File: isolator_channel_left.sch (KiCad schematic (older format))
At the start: 44 parts, among them U201 NE5532, U202 NE5532, U203 NE5532, U204 NE5532

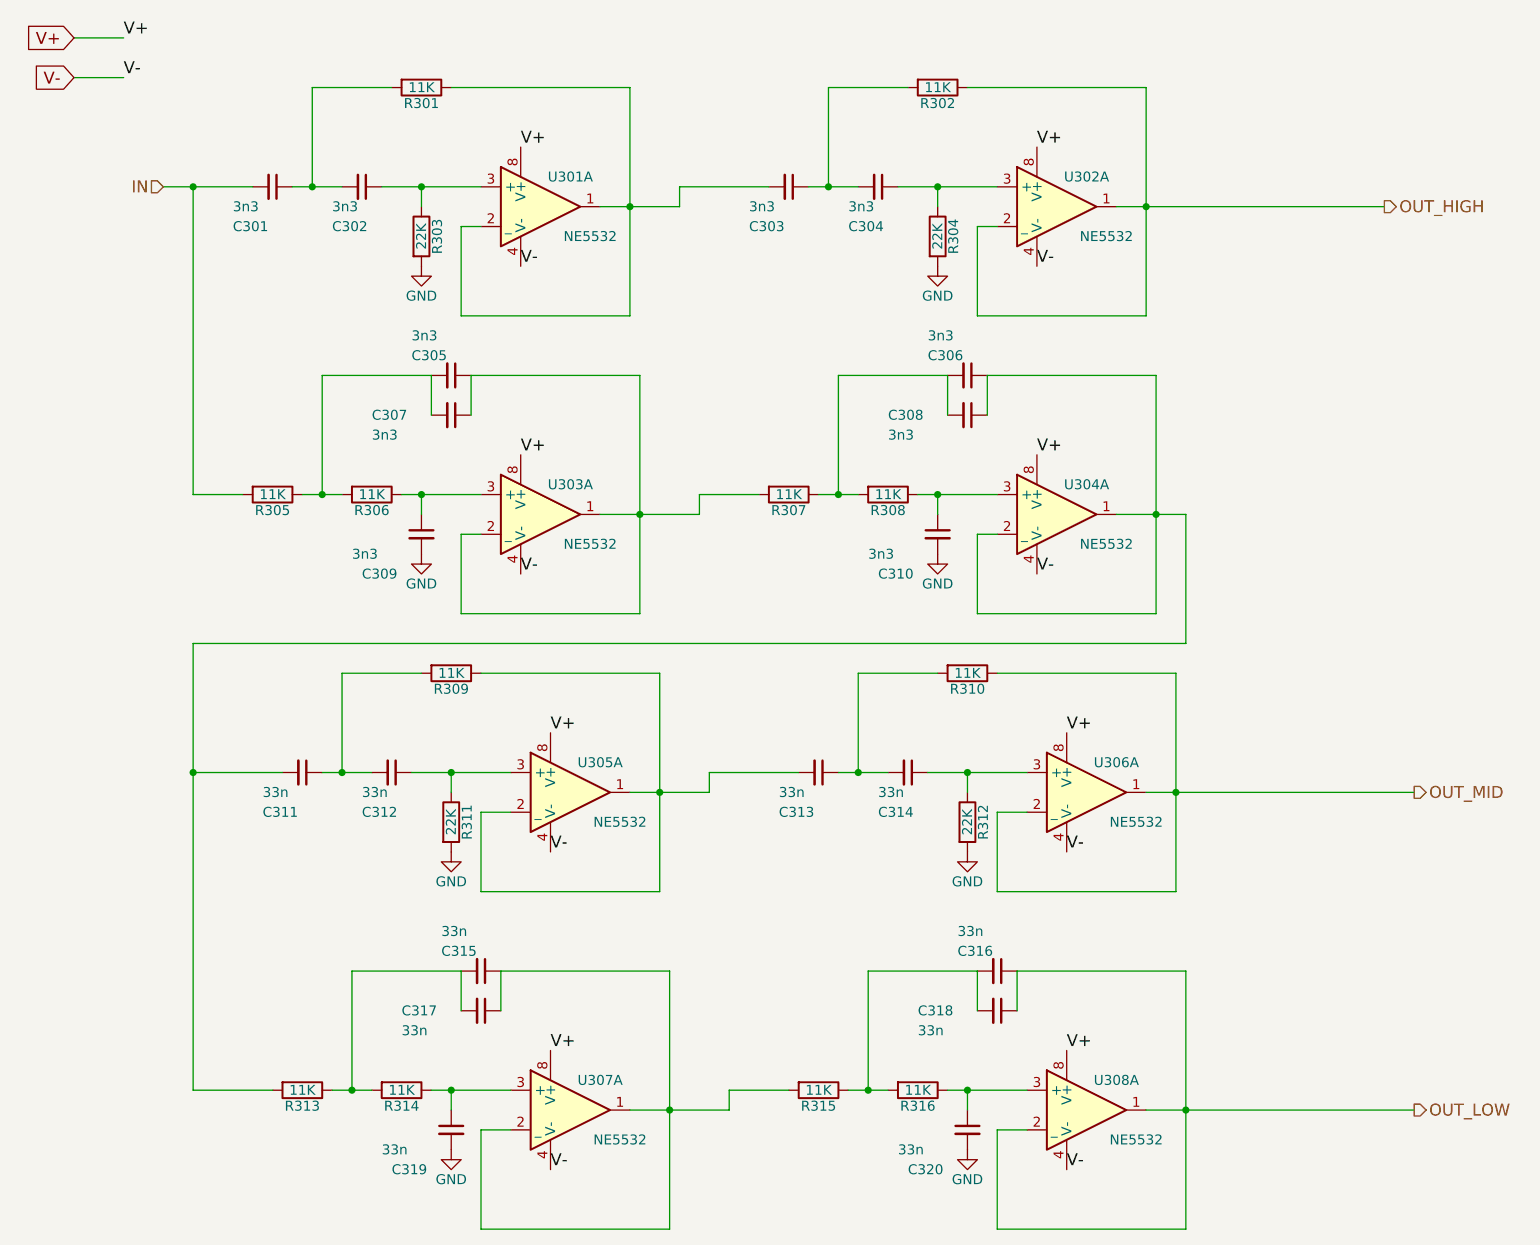
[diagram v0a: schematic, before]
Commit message: Adding active components references
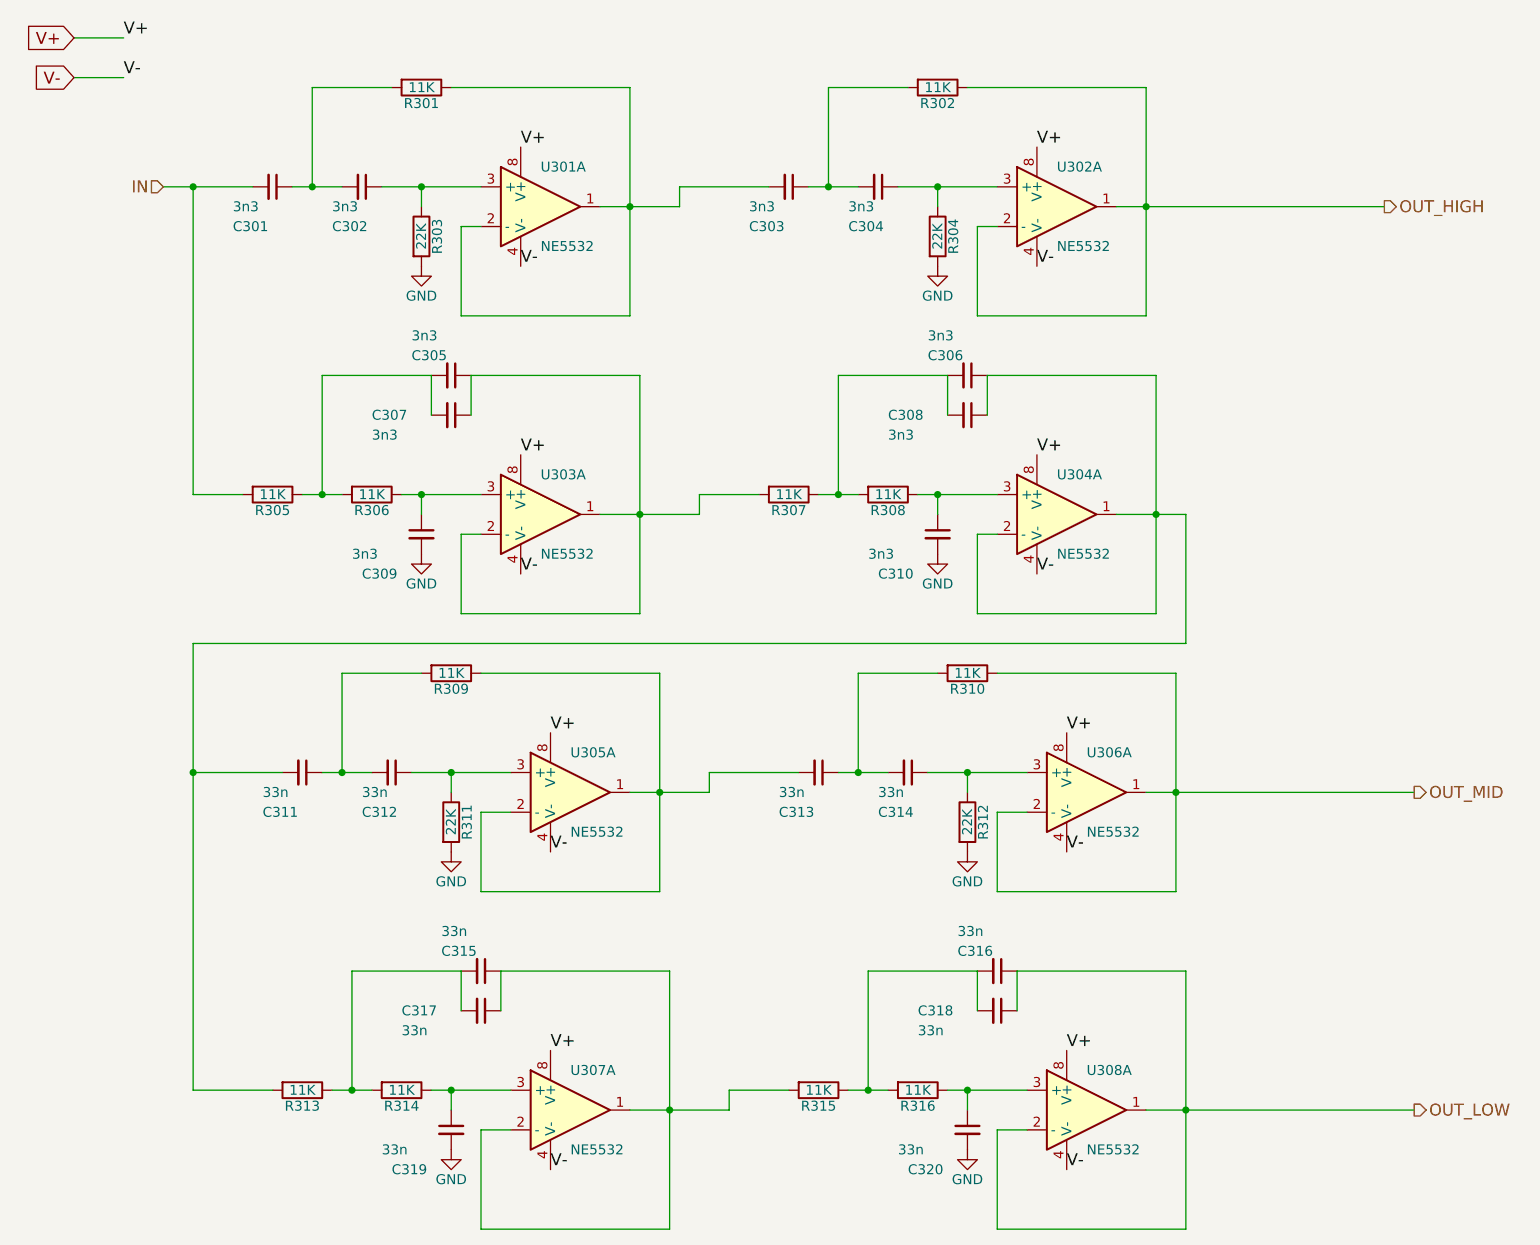
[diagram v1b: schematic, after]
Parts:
- removed U201 (x2), U202 (x2), U203 (x2), U204 (x2): NE5532, Housings_DIP:DIP-8_W7.62mm_LongPads, symbol NE5532-RESCUE-isolator
- added U301, U302, U303, U304, U305, U306, U307, U308: NE5532, Housings_DIP:DIP-8_W7.62mm_LongPads, symbol NE5532
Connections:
- net OUT_HIGH: now also U302.1, U302.2 (-)
- net OUT_LOW: now also U308.1, U308.2 (-)
- net OUT_MID: now also U306.1, U306.2 (-)
- net V+: now also U301.8 (V+), U302.8 (V+), U303.8 (V+), U304.8 (V+), U305.8 (V+), U306.8 (V+), U307.8 (V+), U308.8 (V+)
- net V-: now also U301.4 (V-), U302.4 (V-), U303.4 (V-), U304.4 (V-), U305.4 (V-), U306.4 (V-), U307.4 (V-), U308.4 (V-)
- net at C202.1, R203.1: now also U301.3 (+)
- net at C204.1, R204.1: now also U302.3 (+)
- net at C203.2, R201.1: now also U301.1, U301.2 (-)
- net at C209.1, R206.1: now also U303.3 (+)
- net at C205.1, C207.1, R207.2: now also U303.1, U303.2 (-)
- net at C210.1, R208.1: now also U304.3 (+)
- net at C206.1, C208.1, C211.2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: now also U304.1, U304.2 (-)
- net at C212.1, R211.1: now also U305.3 (+)
- net at C214.1, R212.1: now also U306.3 (+)
- net at C213.2, R209.1: now also U305.1, U305.2 (-)
- net at C219.1, R214.1: now also U307.3 (+)
- net at C215.1, C217.1, R215.2: now also U307.1, U307.2 (-)
- net at C220.1, R216.1: now also U308.3 (+)
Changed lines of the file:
@@
 Text HLabel 7650 6150 2    60   Output ~ 0
 OUT_LOW
-$Comp
-L NE5532-RESCUE-isolator U201
-U 1 1 5707D56E
-P 3250 1600
-AR Path="/56D7589A/5707D56E" Ref="U201"  Part="1"
-AR Path="/56D7630B/5707D56E" Ref="U301"  Part="1"
-AR Path="/5707D56E" Ref="U301"  Part="1"
-F 0 "U301" H 3400 1750 50  0000 C CNN
-F 1 "NE5532" H 3500 1450 50  0000 C CNN
-F 2 "Housings_DIP:DIP-8_W7.62mm_LongPads" H 3250 1600 50  0001 C CNN
-F 3 "" H 3250 1600 50  0000 C CNN
-F 4 "NE5532P" H 3250 1600 60  0001 C CNN "Mfg_Part_No"
-	1    3250 1600
-	1    0    0    -1
-$EndComp
-$Comp
-L NE5532-RESCUE-isolator U201
-U 1 1 5707D56F
-P 5850 1600
-AR Path="/56D7589A/5707D56F" Ref="U201"  Part="2"
-AR Path="/56D7630B/5707D56F" Ref="U302"  Part="1"
-AR Path="/5707D56F" Ref="U302"  Part="1"
-F 0 "U302" H 6000 1750 50  0000 C CNN
-F 1 "NE5532" H 6100 1450 50  0000 C CNN
-F 2 "Housings_DIP:DIP-8_W7.62mm_LongPads" H 5850 1600 50  0001 C CNN
-F 3 "" H 5850 1600 50  0000 C CNN
-F 4 "NE5532P" H 5850 1600 60  0001 C CNN "Mfg_Part_No"
-	1    5850 1600
-	1    0    0    -1
-$EndComp
-$Comp
-L NE5532-RESCUE-isolator U202
-U 1 1 5707D570
-P 3250 3150
-AR Path="/56D7589A/5707D570" Ref="U202"  Part="1"
-AR Path="/56D7630B/5707D570" Ref="U303"  Part="1"
-AR Path="/5707D570" Ref="U303"  Part="1"
-F 0 "U303" H 3400 3300 50  0000 C CNN
-F 1 "NE5532" H 3500 3000 50  0000 C CNN
-F 2 "Housings_DIP:DIP-8_W7.62mm_LongPads" H 3250 3150 50  0001 C CNN
-F 3 "" H 3250 3150 50  0000 C CNN
-F 4 "NE5532P" H 3250 3150 60  0001 C CNN "Mfg_Part_No"
-	1    3250 3150
-	1    0    0    -1
-$EndComp
-$Comp
-L NE5532-RESCUE-isolator U202
-U 1 1 56D77823
-P 5850 3150
-AR Path="/56D7589A/56D77823" Ref="U202"  Part="2"
-AR Path="/56D7630B/56D77823" Ref="U304"  Part="1"
-AR Path="/56D77823" Ref="U304"  Part="1"
-F 0 "U304" H 6000 3300 50  0000 C CNN
-F 1 "NE5532" H 6100 3000 50  0000 C CNN
-F 2 "Housings_DIP:DIP-8_W7.62mm_LongPads" H 5850 3150 50  0001 C CNN
-F 3 "" H 5850 3150 50  0000 C CNN
-F 4 "NE5532P" H 5850 3150 60  0001 C CNN "Mfg_Part_No"
-	1    5850 3150
-	1    0    0    -1
-$EndComp
-$Comp
-L NE5532-RESCUE-isolator U203
-U 1 1 56D778B4
-P 6000 4550
-AR Path="/56D7589A/56D778B4" Ref="U203"  Part="2"
-AR Path="/56D7630B/56D778B4" Ref="U306"  Part="1"
-AR Path="/56D778B4" Ref="U306"  Part="1"
-F 0 "U306" H 6150 4700 50  0000 C CNN
-F 1 "NE5532" H 6250 4400 50  0000 C CNN
-F 2 "Housings_DIP:DIP-8_W7.62mm_LongPads" H 6000 4550 50  0001 C CNN
-F 3 "" H 6000 4550 50  0000 C CNN
-F 4 "NE5532P" H 6000 4550 60  0001 C CNN "Mfg_Part_No"
-	1    6000 4550
-	1    0    0    -1
-$EndComp
-$Comp
-L NE5532-RESCUE-isolator U203
-U 1 1 56D77A2A
-P 3400 4550
-AR Path="/56D7589A/56D77A2A" Ref="U203"  Part="1"
-AR Path="/56D7630B/56D77A2A" Ref="U305"  Part="1"
-AR Path="/56D77A2A" Ref="U305"  Part="1"
-F 0 "U305" H 3550 4700 50  0000 C CNN
-F 1 "NE5532" H 3650 4400 50  0000 C CNN
-F 2 "Housings_DIP:DIP-8_W7.62mm_LongPads" H 3400 4550 50  0001 C CNN
-F 3 "" H 3400 4550 50  0000 C CNN
-F 4 "NE5532P" H 3400 4550 60  0001 C CNN "Mfg_Part_No"
-	1    3400 4550
-	1    0    0    -1
-$EndComp
-$Comp
-L NE5532-RESCUE-isolator U204
-U 1 1 56D77AC1
-P 3400 6150
-AR Path="/56D7589A/56D77AC1" Ref="U204"  Part="1"
-AR Path="/56D7630B/56D77AC1" Ref="U307"  Part="1"
-AR Path="/56D77AC1" Ref="U307"  Part="1"
-F 0 "U307" H 3550 6300 50  0000 C CNN
-F 1 "NE5532" H 3650 6000 50  0000 C CNN
-F 2 "Housings_DIP:DIP-8_W7.62mm_LongPads" H 3400 6150 50  0001 C CNN
-F 3 "" H 3400 6150 50  0000 C CNN
-F 4 "NE5532P" H 3400 6150 60  0001 C CNN "Mfg_Part_No"
-	1    3400 6150
-	1    0    0    -1
-$EndComp
-$Comp
-L NE5532-RESCUE-isolator U204
-U 1 1 5707D575
-P 6000 6150
-AR Path="/56D7589A/5707D575" Ref="U204"  Part="2"
-AR Path="/56D7630B/5707D575" Ref="U308"  Part="1"
-AR Path="/5707D575" Ref="U308"  Part="1"
-F 0 "U308" H 6150 6300 50  0000 C CNN
-F 1 "NE5532" H 6250 6000 50  0000 C CNN
-F 2 "Housings_DIP:DIP-8_W7.62mm_LongPads" H 6000 6150 50  0001 C CNN
-F 3 "" H 6000 6150 50  0000 C CNN
-F 4 "NE5532P" H 6000 6150 60  0001 C CNN "Mfg_Part_No"
-	1    6000 6150
-	1    0    0    -1
-$EndComp
 Text Label 3150 1300 0    60   ~ 0
 V+
@@
 Wire Wire Line
 	1150 750  900  750
+$Comp
+L NE5532 U301
+U 1 1 5A0D9B0B
+P 3250 1600
+F 0 "U301" H 3250 1800 50  0000 L CNN
+F 1 "NE5532" H 3250 1400 50  0000 L CNN
+F 2 "Housings_DIP:DIP-8_W7.62mm_LongPads" H 3250 1600 50  0001 C CNN
+F 3 "http://www.ti.com/lit/gpn/ne5532" H 3250 1600 50  0001 C CNN
+F 4 "NE5532P" H 3250 1600 60  0001 C CNN "Mfg_Part_#"
+F 5 "Mouser" H 3250 1600 60  0001 C CNN "Distributor"
+F 6 "595-NE5532P" H 3250 1600 60  0001 C CNN "Distributor Part #"
+F 7 "8-PDIP" H 3250 1600 60  0001 C CNN "Package"
+F 8 "Amplificateurs opérationnels - Amplis-Op Dual Low Noise" H 3250 1600 60  0001 C CNN "Description"
+F 9 "Texas Instruments" H 3250 1600 60  0001 C CNN "Manufacturer"
+	1    3250 1600
+	1    0    0    -1
+$EndComp
+$Comp
+L NE5532 U302
+U 1 1 5A0D9B6E
+P 5850 1600
+F 0 "U302" H 5850 1800 50  0000 L CNN
+F 1 "NE5532" H 5850 1400 50  0000 L CNN
+F 2 "Housings_DIP:DIP-8_W7.62mm_LongPads" H 5850 1600 50  0001 C CNN
+F 3 "http://www.ti.com/lit/gpn/ne5532" H 5850 1600 50  0001 C CNN
+F 4 "NE5532P" H 5850 1600 60  0001 C CNN "Mfg_Part_#"
+F 5 "Mouser" H 5850 1600 60  0001 C CNN "Distributor"
+F 6 "595-NE5532P" H 5850 1600 60  0001 C CNN "Distributor Part #"
+F 7 "8-PDIP" H 5850 1600 60  0001 C CNN "Package"
+F 8 "Amplificateurs opérationnels - Amplis-Op Dual Low Noise" H 5850 1600 60  0001 C CNN "Description"
+F 9 "Texas Instruments" H 5850 1600 60  0001 C CNN "Manufacturer"
+	1    5850 1600
+	1    0    0    -1
+$EndComp
+$Comp
+L NE5532 U303
+U 1 1 5A0D9C6A
+P 3250 3150
+F 0 "U303" H 3250 3350 50  0000 L CNN
+F 1 "NE5532" H 3250 2950 50  0000 L CNN
+F 2 "Housings_DIP:DIP-8_W7.62mm_LongPads" H 3250 3150 50  0001 C CNN
+F 3 "http://www.ti.com/lit/gpn/ne5532" H 3250 3150 50  0001 C CNN
+F 4 "NE5532P" H 3250 3150 60  0001 C CNN "Mfg_Part_#"
+F 5 "Mouser" H 3250 3150 60  0001 C CNN "Distributor"
+F 6 "595-NE5532P" H 3250 3150 60  0001 C CNN "Distributor Part #"
+F 7 "8-PDIP" H 3250 3150 60  0001 C CNN "Package"
+F 8 "Amplificateurs opérationnels - Amplis-Op Dual Low Noise" H 3250 3150 60  0001 C CNN "Description"
+F 9 "Texas Instruments" H 3250 3150 60  0001 C CNN "Manufacturer"
+	1    3250 3150
+	1    0    0    -1
+$EndComp
+$Comp
+L NE5532 U304
+U 1 1 5A0D9D12
+P 5850 3150
+F 0 "U304" H 5850 3350 50  0000 L CNN
+F 1 "NE5532" H 5850 2950 50  0000 L CNN
+F 2 "Housings_DIP:DIP-8_W7.62mm_LongPads" H 5850 3150 50  0001 C CNN
+F 3 "http://www.ti.com/lit/gpn/ne5532" H 5850 3150 50  0001 C CNN
+F 4 "NE5532P" H 5850 3150 60  0001 C CNN "Mfg_Part_#"
+F 5 "Mouser" H 5850 3150 60  0001 C CNN "Distributor"
+F 6 "595-NE5532P" H 5850 3150 60  0001 C CNN "Distributor Part #"
+F 7 "8-PDIP" H 5850 3150 60  0001 C CNN "Package"
+F 8 "Amplificateurs opérationnels - Amplis-Op Dual Low Noise" H 5850 3150 60  0001 C CNN "Description"
+F 9 "Texas Instruments" H 5850 3150 60  0001 C CNN "Manufacturer"
+	1    5850 3150
+	1    0    0    -1
+$EndComp
+$Comp
+L NE5532 U305
+U 1 1 5A0DA1AA
+P 3400 4550
+F 0 "U305" H 3400 4750 50  0000 L CNN
+F 1 "NE5532" H 3400 4350 50  0000 L CNN
+F 2 "Housings_DIP:DIP-8_W7.62mm_LongPads" H 3400 4550 50  0001 C CNN
+F 3 "http://www.ti.com/lit/gpn/ne5532" H 3400 4550 50  0001 C CNN
+F 4 "NE5532P" H 3400 4550 60  0001 C CNN "Mfg_Part_#"
+F 5 "Mouser" H 3400 4550 60  0001 C CNN "Distributor"
+F 6 "595-NE5532P" H 3400 4550 60  0001 C CNN "Distributor Part #"
+F 7 "8-PDIP" H 3400 4550 60  0001 C CNN "Package"
+F 8 "Amplificateurs opérationnels - Amplis-Op Dual Low Noise" H 3400 4550 60  0001 C CNN "Description"
+F 9 "Texas Instruments" H 3400 4550 60  0001 C CNN "Manufacturer"
+	1    3400 4550
+	1    0    0    -1
+$EndComp
+$Comp
+L NE5532 U306
+U 1 1 5A0DA24E
+P 6000 4550
+F 0 "U306" H 6000 4750 50  0000 L CNN
+F 1 "NE5532" H 6000 4350 50  0000 L CNN
+F 2 "Housings_DIP:DIP-8_W7.62mm_LongPads" H 6000 4550 50  0001 C CNN
+F 3 "http://www.ti.com/lit/gpn/ne5532" H 6000 4550 50  0001 C CNN
+F 4 "NE5532P" H 6000 4550 60  0001 C CNN "Mfg_Part_#"
+F 5 "Mouser" H 6000 4550 60  0001 C CNN "Distributor"
+F 6 "595-NE5532P" H 6000 4550 60  0001 C CNN "Distributor Part #"
+F 7 "8-PDIP" H 6000 4550 60  0001 C CNN "Package"
+F 8 "Amplificateurs opérationnels - Amplis-Op Dual Low Noise" H 6000 4550 60  0001 C CNN "Description"
+F 9 "Texas Instruments" H 6000 4550 60  0001 C CNN "Manufacturer"
+	1    6000 4550
+	1    0    0    -1
+$EndComp
+$Comp
+L NE5532 U307
+U 1 1 5A0DA49E
+P 3400 6150
+F 0 "U307" H 3400 6350 50  0000 L CNN
+F 1 "NE5532" H 3400 5950 50  0000 L CNN
+F 2 "Housings_DIP:DIP-8_W7.62mm_LongPads" H 3400 6150 50  0001 C CNN
+F 3 "http://www.ti.com/lit/gpn/ne5532" H 3400 6150 50  0001 C CNN
+F 4 "NE5532P" H 3400 6150 60  0001 C CNN "Mfg_Part_#"
+F 5 "Mouser" H 3400 6150 60  0001 C CNN "Distributor"
+F 6 "595-NE5532P" H 3400 6150 60  0001 C CNN "Distributor Part #"
+F 7 "8-PDIP" H 3400 6150 60  0001 C CNN "Package"
+F 8 "Amplificateurs opérationnels - Amplis-Op Dual Low Noise" H 3400 6150 60  0001 C CNN "Description"
+F 9 "Texas Instruments" H 3400 6150 60  0001 C CNN "Manufacturer"
+	1    3400 6150
+	1    0    0    -1
+$EndComp
+$Comp
+L NE5532 U308
+U 1 1 5A0DA545
+P 6000 6150
+F 0 "U308" H 6000 6350 50  0000 L CNN
+F 1 "NE5532" H 6000 5950 50  0000 L CNN
+F 2 "Housings_DIP:DIP-8_W7.62mm_LongPads" H 6000 6150 50  0001 C CNN
+F 3 "http://www.ti.com/lit/gpn/ne5532" H 6000 6150 50  0001 C CNN
+F 4 "NE5532P" H 6000 6150 60  0001 C CNN "Mfg_Part_#"
+F 5 "Mouser" H 6000 6150 60  0001 C CNN "Distributor"
+F 6 "595-NE5532P" H 6000 6150 60  0001 C CNN "Distributor Part #"
+F 7 "8-PDIP" H 6000 6150 60  0001 C CNN "Package"
+F 8 "Amplificateurs opérationnels - Amplis-Op Dual Low Noise" H 6000 6150 60  0001 C CNN "Description"
+F 9 "Texas Instruments" H 6000 6150 60  0001 C CNN "Manufacturer"
+	1    6000 6150
+	1    0    0    -1
+$EndComp
 $EndSCHEMATC

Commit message: Updating components references and properties
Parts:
- C201, C202, C203, C204, C205, C206, C207, C208, C209, C210, C211, C212, C213, C214, C215, C216, C217, C218, C219, C220: footprint Capacitors_ThroughHole:C_Rect_L7_W3.5_P5 -> Capacitors_THT:C_Rect_L7.0mm_W3.5mm_P5.00mm
- R201, R202, R203, R204, R205, R206, R207, R208, R209, R210, R211, R212, R213, R214, R215, R216: footprint Resistors_ThroughHole:Resistor_Horizontal_RM7mm -> Resistors_THT:R_Axial_DIN0204_L3.6mm_D1.6mm_P5.08mm_Horizontal
